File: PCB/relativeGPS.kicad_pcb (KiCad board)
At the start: 2 copper layers, 3 parts, among them CN1 PPPC051LGBN-RC, U1 TCA39306DCUR, U2 LSM303AH

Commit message: WIP
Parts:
- added ANT1: ANT2525B00DT1516S, 010-RF:ANT2525B00DT1516S, F.Cu at (139.9, 80.5)
- added C1: C_120pF_50V_5%_C0G_0402_H0.55, 002-Capacitors:C_0402_H0.55, F.Cu at (154.6, 68.3)
- added C10: C_1uF_50V_10%_X5R_0603_H0.9, 002-Capacitors:C_0603_H0.95, F.Cu at (173.0, 71.1)
- added C11: C_1uF_50V_10%_X5R_0603_H0.9, 002-Capacitors:C_0603_H0.95, F.Cu at (173.0, 73.6)
- added C12: C_100nF_50V_10%_X7R_0402_H0.55, 002-Capacitors:C_0402_H0.55, F.Cu at (163.7, 89.3)
- added C13: C_220nF_50V_10%_X7R_0603_H0.9, 002-Capacitors:C_0603_H0.95, F.Cu at (160.2, 87.5)
- added C14: C_10uF_10V_20%_X5R_0603H0.9, 002-Capacitors:C_0603_H0.95, F.Cu at (160.2, 90.0)
- added C2: C_4.7uF_10V_10%_X7S_0603_H0.95, 002-Capacitors:C_0603_H0.95, F.Cu at (148.5, 95.0)
- added C3: C_22uF_6.3V_20%_X5R_0805_H1.4, 002-Capacitors:C_0805_H1.4, F.Cu at (152.7, 95.2)
- added C4: C_120pF_50V_5%_C0G_0402_H0.55, 002-Capacitors:C_0402_H0.55, F.Cu at (154.6, 70.4)
- added C5: C_10nF_50V_10%_X7R_0402_H0.55, 002-Capacitors:C_0402_H0.55, F.Cu at (154.6, 72.5)
- added C6: C_56pF_50V_2%_C0G_0201_H0.33, 002-Capacitors:C_0402_H0.55, F.Cu at (154.6, 74.5)
- added C7: C_100nF_50V_10%_X7R_0402_H0.55, 002-Capacitors:C_0402_H0.55, F.Cu at (163.7, 87.3)
- added C8: C_100nF_50V_10%_X7R_0402_H0.55, 002-Capacitors:C_0402_H0.55, F.Cu at (159.7, 83.2)
- added C9: C_1uF_50V_10%_X5R_0603_H0.9, 002-Capacitors:C_0603_H0.95, F.Cu at (173.0, 68.6)
- added CN2: Solder_Jumper-2_Open, 009-Connectors:SolderJumper-2_Open, F.Cu at (148.7, 100.5)
- added IC1: MIC5330-SSYML-TR, 004-Power:MIC5330, F.Cu at (173.1, 81.8)
- added L1: L_5.6nH_2%_1.77A_40mOhm, 003-Inductors:LQW15AN5N6G80D, F.Cu at (152.3, 99.9)
- added L2: L_10uH_20%_1.51A_160mOhm, 003-Inductors:LTF5022T-100M1R3-D, F.Cu at (142.5, 97.1)
- added L3: L_27nH_5%_0.35A_460mOhm, 003-Inductors:LQG15HS27NJ02D, F.Cu at (152.2, 102.0)
- added R1: R_1M_5%_1/16W_0402, 001-Resistors:R_0402_H0.4, F.Cu at (154.6, 76.5)
- added R10: R_4k7_1%_1/10W_0603, 001-Resistors:R_0603_H0.55, F.Cu at (173.0, 78.6)
- added R2: R_0R_0603, 001-Resistors:R_0603_H0.55, F.Cu at (148.5, 97.5)
- added R3: R_68k_1%_1/16W_0402, 001-Resistors:R_0402_H0.4, F.Cu at (154.6, 78.6)
- added R4: R_15k_1%_1/16W_0402, 001-Resistors:R_0402_H0.4, F.Cu at (154.6, 80.7)
- added R5: R_4k7_1%_1/10W_0603, 001-Resistors:R_0603_H0.55, F.Cu at (160.2, 92.5)
- added R6: R_10k_5%_1/16W_0402, 001-Resistors:R_0402_H0.4, F.Cu at (154.6, 82.7)
- added R7: R_4k7_1%_1/10W_0603, 001-Resistors:R_0603_H0.55, F.Cu at (160.2, 95.1)
- added R8: R_200k_1%_1/16W_0402, 001-Resistors:R_0402_H0.4, F.Cu at (163.7, 91.4)
- added R9: R_4k7_1%_1/10W_0603, 001-Resistors:R_0603_H0.55, F.Cu at (173.0, 76.1)
- added U3: BGA725L6E6327FTSA1, 010-RF:BGA725L6E6327FTSA1, F.Cu at (152.2, 104.2)
- added U4: ST1S12GR, 004-Power:ST1S12GR, F.Cu at (140.7, 103.0)
- added U5: B39162B4327P810, 010-RF:B39162B4327P810, F.Cu at (148.0, 103.6)
- added U6: TESEO-LIV3R, 010-RF:TESEO-LIV3R, F.Cu at (132.5, 99.9)
- U1: value TCA39306DCUR -> LSM303AH; footprint 005-ICs:TCA39306DCUR -> 008-Sensors:LSM303AHTR
- U2: value LSM303AH -> TCA39306DCUR; footprint 008-Sensors:LSM303AHTR -> 005-ICs:TCA39306DCUR
- moved U1 30.4 mm to (167.1, 88.2)
- moved U2 28.1 mm to (164.9, 94.2)
- moved CN1 22.0 mm to (160.0, 74.8)
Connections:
- net /SDA_1V8 renamed /MAG_ACC/LSM_SDA
- CN1 pad 1: +3.3V -> +3.3V_RYLR
- U1 pad 1: GND -> /MAG_ACC/LSM_SCL
- U1 pad 3: /SCL_1V8 -> unconnected-(U1-NC-Pad3)
- U1 pad 5: unconnected-(U1-SDA2-Pad5) -> Net-(U1-C1)
- U1 pad 6: unconnected-(U1-SCL2-Pad6) -> GND
- U1 pad 7: unconnected-(U1-VREF2-Pad7) -> /MAG_ACC_DRDY
- U1 pad 8: unconnected-(U1-EN-Pad8) -> GND
- U2 pad 1: /SCL_1V8 -> GND
- U2 pad 3: unconnected-(U2-NC-Pad3) -> /MAG_ACC/LSM_SCL
- U2 pad 5: unconnected-(U2-C1-Pad5) -> /SDA
- U2 pad 6: GND -> /SCL
- U2 pad 7: unconnected-(U2-DRDY/MAG_INT-Pad7) -> Net-(U2-EN)
- U2 pad 8: GND -> Net-(U2-EN)

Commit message: WIP
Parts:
- added U7: AAA_2X_Holder, 004-Power:AAA_2X_Holder, B.Cu at (147.8, 100.0)
- C6, U6: moved to B.Cu
- C8: value C_100nF_50V_10%_X7R_0402_H0.55 -> C_1uF_50V_10%_X5R_0603_H0.9; footprint 002-Capacitors:C_0402_H0.55 -> 002-Capacitors:C_0603_H0.95
- C9: value C_1uF_50V_10%_X5R_0603_H0.9 -> C_100nF_50V_10%_X7R_0402_H0.55; footprint 002-Capacitors:C_0603_H0.95 -> 002-Capacitors:C_0402_H0.55
- CN1: value PPPC051LGBN-RC -> 5PTH_connector; footprint 009-Connectors:PPPC051LGBN-RC -> 009-Connectors:5-PTH_connector
- moved C1 85.1 mm to (239.1, 78.6)
- moved C10 85.1 mm to (257.5, 81.3)
- moved C11 85.1 mm to (257.5, 83.8)
- moved C12 85.1 mm to (248.2, 99.6)
- moved C13 85.1 mm to (244.6, 97.8)
- moved C14 85.1 mm to (244.6, 100.3)
- moved C3 85.1 mm to (237.2, 105.5)
- moved C4 85.1 mm to (239.1, 80.6)
- moved C5 85.1 mm to (239.1, 82.7)
- moved C7 85.1 mm to (248.2, 97.5)
- moved C8 85.1 mm to (244.1, 93.5)
- moved C9 85.1 mm to (257.5, 78.8)
- moved CN2 85.1 mm to (233.1, 110.8)
- moved IC1 85.1 mm to (257.5, 92.0)
- moved L1 85.1 mm to (236.8, 110.1)
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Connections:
- C8 pad 1: Net-(IC1-BYP) -> +5V
- C9 pad 1: +5V -> Net-(IC1-BYP)
- IC1 pad 9: (no net) -> GND
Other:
- board outline added: 60 x 60 mm

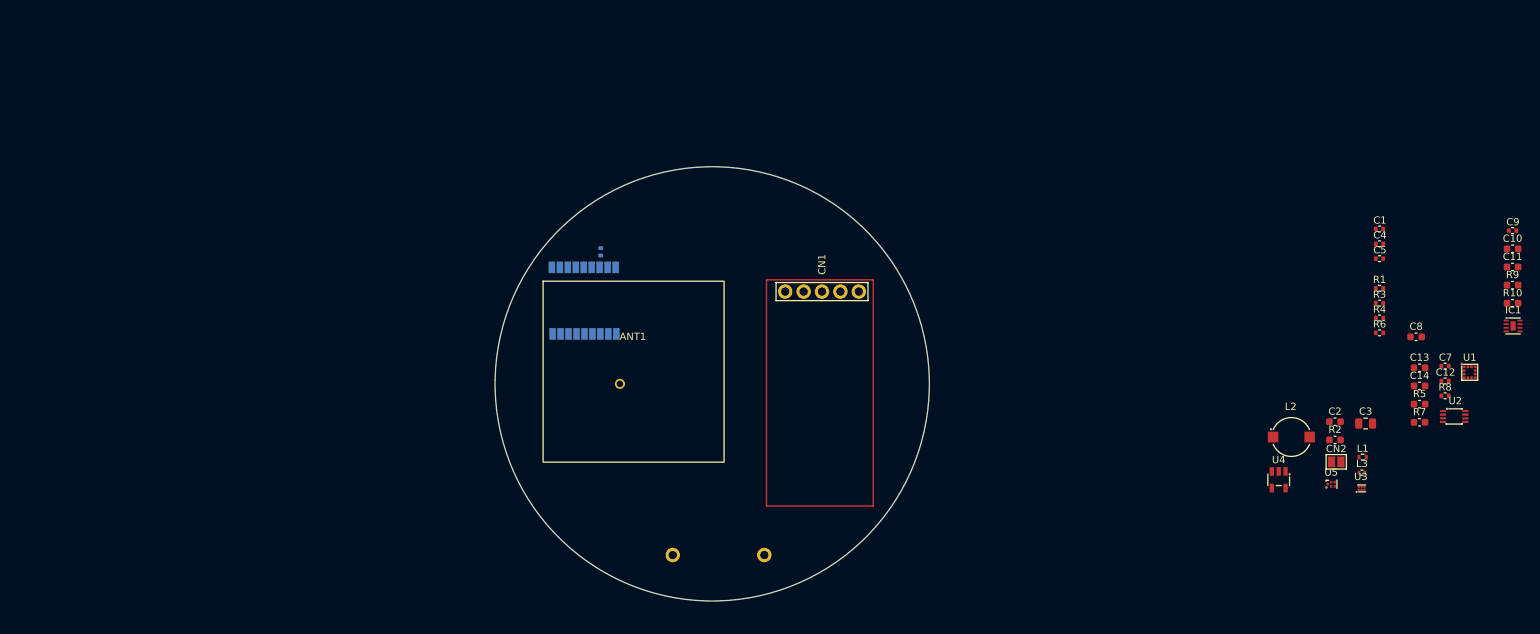
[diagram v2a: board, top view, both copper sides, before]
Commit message: Add LEDs
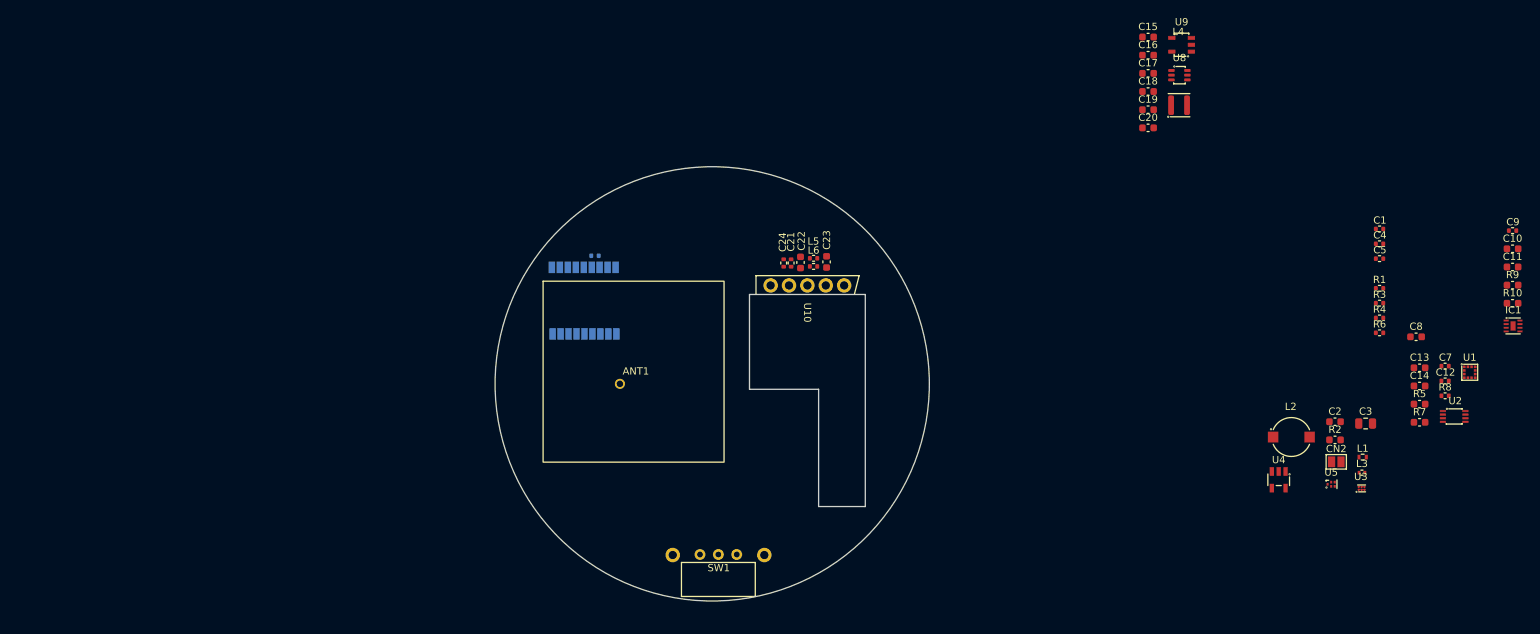
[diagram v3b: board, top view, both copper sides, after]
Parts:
- removed CN1: 5PTH_connector, 009-Connectors:5-PTH_connector
- added C15: C_4.7uF_10V_10%_X7S_0603_H0.95, 002-Capacitors:C_0603_H0.95, F.Cu at (207.1, 52.1)
- added C16: C_1uF_50V_10%_X5R_0603_H0.9, 002-Capacitors:C_0603_H0.95, F.Cu at (207.1, 54.6)
- added C17: C_10uF_10V_20%_X5R_0603H0.9, 002-Capacitors:C_0603_H0.95, F.Cu at (207.1, 57.1)
- added C18: C_100pF_50V_5%_C0G_0603_H0.9, 002-Capacitors:C_0603_H0.95, F.Cu at (207.1, 59.6)
- added C19: C_22uF_25V_20%_X5S_0603_H1, 002-Capacitors:C_0603_H0.95, F.Cu at (207.1, 62.1)
- added C20: C_22uF_25V_20%_X5S_0603_H1, 002-Capacitors:C_0603_H0.95, F.Cu at (207.1, 64.6)
- added C21: C_100nF_50V_10%_X7R_0402_H0.55, 002-Capacitors:C_0402_H0.55, F.Cu at (157.8, 83.3)
- added C22: C_10uF_10V_20%_X5R_0603H0.9, 002-Capacitors:C_0603_H0.95, F.Cu at (159.1, 83.2)
- added C23: C_10uF_10V_20%_X5R_0603H0.9, 002-Capacitors:C_0603_H0.95, F.Cu at (162.7, 83.2)
- added C24: C_47pF_50V_5%_C0G_0402, 002-Capacitors:C_0402_H0.55, F.Cu at (156.8, 83.3)
- added L4: L_4.7uH_20%_850mA_168mOhm, 003-Inductors:LQH3NPZ4R7MGRL, F.Cu at (211.4, 61.5)
- added L5: FERR_120R@100MHz_5%_1.5A_95mOhm, 003-Inductors:FERR_0402_H0.55, F.Cu at (160.9, 82.7)
- added L6: FERR_120R@100MHz_5%_1.5A_95mOhm, 003-Inductors:FERR_0402_H0.55, F.Cu at (160.9, 83.8)
- added SW1: switch_slide_2pos, 009-Connectors:09.10290.01, F.Cu at (147.8, 123.6)
- added U10: RYLR998, 010-RF:RYLR998_flat, F.Cu at (160.1, 86.4)
- added U8: TPS61222DCKR, 004-Power:TPS61222DCKR, F.Cu at (211.4, 57.4)
- added U9: TPS79318DBVR, 004-Power:TPS79318DBVR, F.Cu at (211.8, 53.1)
- moved C6 0.97 mm to (130.7, 82.3), turned to 180 degrees
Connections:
- net /GPS/3V3_TESEO renamed +3.3V_TESEO
- net /RYLR_3V3_EN renamed /3V3_RYLR_EN

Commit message: WIP
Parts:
- added C25: C_22uF_25V_20%_X5S_0603_H1, 002-Capacitors:C_0603_H0.95, F.Cu at (106.0, 69.2)
- added C26: C_2.2uF_25V_25%_X5R_0402_H0.55, 002-Capacitors:C_0402_H0.55, F.Cu at (88.1, 97.1)
- added C27: C_100nF_50V_10%_X7R_0402_H0.55, 002-Capacitors:C_0402_H0.55, F.Cu at (88.1, 99.2)
- added CN1: FTSH-107-01-L-DV-K-P-TR, 009-Connectors:FTSH-107-01-L-DV-K-P-TR, F.Cu at (103.2, 100.3)
- added CN3: TC2030-IDC, 009-Connectors:Debug_pads_6pin, F.Cu at (104.4, 107.3)
- added CN4: 5033981892, 009-Connectors:Micro_SD_5033981892, F.Cu at (79.0, 104.0)
- added D1: COM-16347, 006-Diodes:COM-16347, F.Cu at (75.5, 71.2)
- added D10: COM-16347, 006-Diodes:COM-16347, F.Cu at (91.4, 77.7)
- added D11: COM-16347, 006-Diodes:COM-16347, F.Cu at (91.4, 84.3)
- added D2: COM-16347, 006-Diodes:COM-16347, F.Cu at (75.5, 77.7)
- added D3: COM-16347, 006-Diodes:COM-16347, F.Cu at (75.5, 84.3)
- added D4: COM-16347, 006-Diodes:COM-16347, F.Cu at (75.5, 90.8)
- added D5: COM-16347, 006-Diodes:COM-16347, F.Cu at (83.4, 71.2)
- added D6: COM-16347, 006-Diodes:COM-16347, F.Cu at (83.4, 77.7)
- added D7: COM-16347, 006-Diodes:COM-16347, F.Cu at (83.4, 84.3)
- added D8: COM-16347, 006-Diodes:COM-16347, F.Cu at (83.4, 90.8)
- added D9: COM-16347, 006-Diodes:COM-16347, F.Cu at (91.4, 71.2)
- added R11: R_100k_1%_1/16W_0402, 001-Resistors:R_0402_H0.4, F.Cu at (88.1, 101.2)
- added R12: R_100k_1%_1/16W_0402, 001-Resistors:R_0402_H0.4, F.Cu at (88.1, 103.3)
- added R13: R_100k_1%_1/16W_0402, 001-Resistors:R_0402_H0.4, F.Cu at (88.1, 105.3)
- added R14: R_100k_1%_1/16W_0402, 001-Resistors:R_0402_H0.4, F.Cu at (88.1, 107.4)
- added SW2: EVQ-P7A01P, 009-Connectors:EVQ-P7A01P, F.Cu at (94.7, 98.5)
- added SW3: EVQ-P7A01P, 009-Connectors:EVQ-P7A01P, F.Cu at (94.7, 103.6)
- added TP1: TP_square_1mm, 011-Misc:Testpoint_square_1mm, F.Cu at (98.9, 105.5)
- added TP10: TP_square_1mm, 011-Misc:Testpoint_square_1mm, F.Cu at (103.0, 70.9)
- added TP11: TP_square_1mm, 011-Misc:Testpoint_square_1mm, F.Cu at (98.9, 107.5)
- added TP12: TP_square_1mm, 011-Misc:Testpoint_square_1mm, F.Cu at (98.9, 109.5)
- added TP2: TP_square_1mm, 011-Misc:Testpoint_square_1mm, F.Cu at (96.4, 72.4)
- added TP3: TP_square_1mm, 011-Misc:Testpoint_square_1mm, F.Cu at (87.6, 109.4)
- added TP4: TP_square_1mm, 011-Misc:Testpoint_square_1mm, F.Cu at (107.0, 74.9)
- added TP5: TP_square_1mm, 011-Misc:Testpoint_square_1mm, F.Cu at (107.0, 76.9)
- added TP6: TP_square_1mm, 011-Misc:Testpoint_square_1mm, F.Cu at (103.0, 74.9)
- added TP7: TP_square_1mm, 011-Misc:Testpoint_square_1mm, F.Cu at (103.0, 76.9)
- added TP8: TP_square_1mm, 011-Misc:Testpoint_square_1mm, F.Cu at (103.0, 78.9)
- added TP9: TP_square_1mm, 011-Misc:Testpoint_square_1mm, F.Cu at (103.0, 68.9)
- added U11: 74LVC1T45GW,125, 005-ICs:TSSOP6_SOT363-2.step, F.Cu at (97.7, 69.7)
- R10, R9: value R_4k7_1%_1/10W_0603 -> R_DNP_0402; footprint 001-Resistors:R_0603_H0.55 -> 001-Resistors:R_0402_H0.4
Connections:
- C11 pad 1: +3.3V_RYLR -> +3.3V
- C15 pad 1: +VBAT -> +3V8
- C16 pad 1: +VBAT_ON -> +3V8
- C20 pad 1: +VBAT_ON -> +3V8
- C23 pad 1: +3.3V_RYLR -> +3.3V
- C3 pad 1: +3.3V_TESEO -> +3.3V
- C5 pad 1: +3.3V_TESEO -> +3.3V
- IC1 pad 7: +3.3V_RYLR -> +3.3V
- L2 pad 2: +3.3V_TESEO -> +3.3V
- L3 pad 1: +3.3V_TESEO -> +3.3V
- L4 pad 1: +VBAT_ON -> +3V8
- L5 pad 1: +3.3V_RYLR -> +3.3V
- R10 pad 2: /SDA -> /SCL
- R9 pad 2: /SCL -> /SDA
- SW1 pad 1: +VBAT_ON -> +3V8
- SW1 pad 2: +VBAT -> +3V8
- U7 pad 1: +VBAT -> +3V8
- U8 pad 1: +VBAT_ON -> +3V8
- U8 pad 6: +VBAT_ON -> +3V8
- U9 pad 1: +VBAT_ON -> +3V8

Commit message: Layout start
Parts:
- removed IC1: MIC5330-SSYML-TR, 004-Power:MIC5330
- removed TP1, TP10, TP11, TP12, TP2, TP3, TP4, TP5, TP6, TP7, TP8, TP9: TP_square_1mm, 011-Misc:Testpoint_square_1mm
- added B7: AAA_2X_Holder, 004-Power:AAA_2X_Holder, B.Cu at (100.0, 99.2)
- added C28: C_10nF_50V_10%_X7R_0402_H0.55, 002-Capacitors:C_0402_H0.55, B.Cu at (70.5, 103.7)
- added C29: C_100nF_50V_10%_X7R_0402_H0.55, 002-Capacitors:C_0402_H0.55, B.Cu at (72.8, 111.4)
- added C30: C_2.2uF_25V_25%_X5R_0402_H0.55, 002-Capacitors:C_0402_H0.55, F.Cu at (109.7, 73.7)
- added C31: C_100nF_50V_10%_X7R_0402_H0.55, 002-Capacitors:C_0402_H0.55, B.Cu at (74.8, 116.2)
- added C32: C_100nF_50V_10%_X7R_0402_H0.55, 002-Capacitors:C_0402_H0.55, B.Cu at (73.4, 109.0)
- added C33: C_100nF_50V_10%_X7R_0402_H0.55, 002-Capacitors:C_0402_H0.55, B.Cu at (77.6, 103.7)
- added C34: C_100nF_50V_10%_X7R_0402_H0.55, 002-Capacitors:C_0402_H0.55, B.Cu at (84.1, 103.7)
- added C35: C_100nF_50V_10%_X7R_0402_H0.55, 002-Capacitors:C_0402_H0.55, B.Cu at (87.9, 114.5)
- added C36: C_10uF_10V_20%_X5R_0402_H0.55, 002-Capacitors:C_0402_H0.55, B.Cu at (88.9, 114.5)
- added R15: R_0R_1%_1/16W_0402, 001-Resistors:R_0402_H0.4, B.Cu at (85.7, 74.0)
- added SW4: TL3315NF160Q, 009-Connectors:TL3315NF160Q, B.Cu at (70.5, 100.0)
- added U12: ASE-8.000MHZ-L-C-T, 005-ICs:ASE-8.000MHZ-L-C-T, B.Cu at (70.6, 106.2)
- added U13: MIC5330-SSYML-TR, 004-Power:MIC5330, F.Cu at (103.9, 112.3)
- C1, C26, C27, C4, C5, CN1, CN2, CN3, L1, L3, R11, R12, R13, R14, R2, R6, U3, U5: moved to B.Cu
- C10, C11, C8: value C_1uF_50V_10%_X5R_0603_H0.9 -> C_1uF_50V_10%_X5R_0402_H0.55; footprint 002-Capacitors:C_0603_H0.95 -> 002-Capacitors:C_0402_H0.55
- C13: value C_220nF_50V_10%_X7R_0603_H0.9 -> C_2.2uF_25V_25%_X5R_0402_H0.55; footprint 002-Capacitors:C_0603_H0.95 -> 002-Capacitors:C_0402_H0.55
- C14: value C_10uF_10V_20%_X5R_0603H0.9 -> C_220nF_16V_10%_X7R_0402_H0.55; footprint 002-Capacitors:C_0603_H0.95 -> 002-Capacitors:C_0402_H0.55
- C17: value C_10uF_10V_20%_X5R_0603H0.9 -> C_100nF_50V_10%_X7R_0402_H0.55; footprint 002-Capacitors:C_0603_H0.95 -> 002-Capacitors:C_0402_H0.55; moved to B.Cu
- R5, R7: value R_4k7_1%_1/10W_0603 -> R_4k7_5%_1/16W_0402; footprint 001-Resistors:R_0603_H0.55 -> 001-Resistors:R_0402_H0.4
- U11: value 74LVC1T45GW,125 -> STM32L431RCT6TR; footprint 005-ICs:TSSOP6_SOT363-2.step -> 007-MCUs:LQFP-64_10x10mm_P0.5mm; moved to B.Cu
- U7: value AAA_2X_Holder -> 74LVC1T45GW.125; footprint 004-Power:AAA_2X_Holder -> 005-ICs:TSSOP6_SOT363-2.step; moved to F.Cu
- moved R9 159.4 mm to (98.5, 74.3), turned to -90 degrees
- moved C10 158.4 mm to (102.0, 111.6), turned to -90 degrees
- moved R10 158.3 mm to (99.7, 76.1), turned to 90 degrees
- moved C9 157.4 mm to (104.1, 114.3), turned to 180 degrees
- moved L3 155.7 mm to (84.8, 77.9), turned to 180 degrees
- moved C1 155.7 mm to (84.8, 99.2), turned to 90 degrees
- moved C11 155.5 mm to (104.2, 110.1)
- moved R6 154.8 mm to (84.3, 91.9), turned to 90 degrees
- moved C4 154.2 mm to (85.3, 91.9), turned to 90 degrees
- moved CN2 153.2 mm to (80.9, 93.5), turned to -90 degrees
- moved U3 152.8 mm to (85.0, 95.6)
- moved C5 152.8 mm to (86.4, 78.4), turned to -90 degrees
- moved L1 152.3 mm to (85.0, 97.2), turned to 90 degrees
- moved R2 150.6 mm to (83.0, 93.5), turned to 90 degrees
- moved U2 149.6 mm to (102.7, 74.9), turned to 180 degrees
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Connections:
- C11 pad 1: +3.3V -> +3.3V_LORA
- C13 pad 1: Net-(U1-C1) -> +1V8
- C14 pad 1: +1V8 -> Net-(U1-C1)
- C15 pad 1: +3V8 -> +BATT
- C16 pad 1: +3V8 -> +3V0
- C17 pad 1: +1V8 -> +3.3V
- C20 pad 1: +3V8 -> +3V0
- C23 pad 1: +3.3V -> +3.3V_LORA
- C3 pad 1: +3.3V -> +3.3V_GPS
- C5 pad 1: +3.3V -> +3.3V_GPS
- CN3 pad 6: /SWO -> unconnected-(CN3-SWO-Pad6)
- CN4 pad 5: /SD_CLK -> Net-(CN4-CLK)
- L2 pad 2: +3.3V -> +3.3V_GPS
- L3 pad 1: +3.3V -> +3.3V_GPS
- L4 pad 1: +3V8 -> +3V0
- L5 pad 1: +3.3V -> +3.3V_LORA
- SW1 pad 1: +3V8 -> unconnected-(SW1-Pad1)
- SW1 pad 2: +3V8 -> +BATT
- SW1 pad 3: unconnected-(SW1-Pad3) -> +3V0
- U11 pad 1: +3V3 -> +3.3V
- U11 pad 2: GND -> unconnected-(U11-PC13-Pad2)
- U11 pad 3: /LED_DATA -> unconnected-(U11-PC14-OSC32_IN-Pad3)
- U11 pad 4: Net-(D1-DIN) -> unconnected-(U11-PC15-OSC32_OUT-Pad4)
- U11 pad 5: +3V3 -> Net-(U11-PH0-OSC_IN)
- U11 pad 6: +5V -> unconnected-(U11-PH1-OSC_OUT-Pad6)
- U7 pad 1: +3V8 -> +3V3
- U8 pad 1: +3V8 -> +3V0
- U8 pad 6: +3V8 -> +3V0
- U9 pad 1: +3V8 -> +3V0
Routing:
- net +5V: track 0.00 -> 227.8 mm, vias 0 -> 4
- net GND: track 0.00 -> 129.8 mm, vias 0 -> 67
- net /NRST: track 0.00 -> 100.7 mm, vias 0 -> 2
- net /UART_TX: track 0.00 -> 87.9 mm, vias 0 -> 4
- net /UART_RX: track 0.00 -> 87.3 mm, vias 0 -> 4
- net /BUTTON_2: track 0.00 -> 84.1 mm, vias 0 -> 1
- net /SWDIO: track 0.00 -> 72.5 mm, vias 0 -> 2
- net /SWCLK: track 0.00 -> 67.4 mm, vias 0 -> 6
- net /SD_DAT3: track 0.00 -> 66.3 mm, vias 0 -> 3
- net /SD_DAT2: track 0.00 -> 63.0 mm, vias 0 -> 3
- net /RYLR998_TX: track 0.00 -> 55.2 mm, vias 0 -> 1
- net /RYLR998_RX: track 0.00 -> 52.7 mm
- net /RYLR998_NRST: track 0.00 -> 50.1 mm
- net /SD_DAT1: track 0.00 -> 45.8 mm, vias 0 -> 1
- net /SD_DAT0: track 0.00 -> 44.6 mm, vias 0 -> 1
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- added copper zone on F.Cu, net +5V
- added copper zone on F.Cu, net GND
- added copper zone on In1.Cu, net GND
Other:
- board size 60 x 60 mm -> 65 x 65 mm
- copper layers 2 -> 4

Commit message: First layout draft
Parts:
- moved C36 15.3 mm to (73.7, 116.2), turned to -90 degrees
- moved C35 2.05 mm to (86.9, 116.3), turned to -90 degrees
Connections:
- C26 pad 1: +3V3 -> +3.3V
- C27 pad 1: +3V3 -> +3.3V
- CN4 pad 4: +3V3 -> +3.3V
- R11 pad 1: +3V3 -> +3.3V
- R12 pad 1: +3V3 -> +3.3V
- R13 pad 1: +3V3 -> +3.3V
- R14 pad 1: +3V3 -> +3.3V
- U11 pad 21: unconnected-(U11-PA5-Pad21) -> /BUTTON_1
- U11 pad 33: unconnected-(U11-PB12-Pad33) -> /3V3_RYLR_EN
- U11 pad 34: unconnected-(U11-PB13-Pad34) -> /MAG_ACC_DRDY
- U11 pad 35: unconnected-(U11-PB14-Pad35) -> /MAG_ACC_INT1
- U11 pad 37: unconnected-(U11-PC6-Pad37) -> /MAG_ACC_INT2
- U11 pad 38: unconnected-(U11-PC7-Pad38) -> /3V3_TESEO_EN
- U11 pad 41: unconnected-(U11-PA8-Pad41) -> /SD_DETECT
- U11 pad 45: unconnected-(U11-PA12-Pad45) -> /1V8_ACC_MAG_EN
- U11 pad 56: /SD_DETECT -> unconnected-(U11-PB4-Pad56)
- U7 pad 1: +3V3 -> +3.3V
- U7 pad 5: +3V3 -> +3.3V
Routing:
- net +3.3V: track 32.3 -> 220.0 mm, vias 6 -> 13
- net /MAG_ACC_INT2: track 0.00 -> 52.5 mm, vias 0 -> 3
- net /MAG_ACC_DRDY: track 0.00 -> 52.5 mm, vias 0 -> 1
- net /MAG_ACC_INT1: track 0.00 -> 50.5 mm, vias 0 -> 3
- net /1V8_ACC_MAG_EN: track 0.00 -> 49.3 mm, vias 0 -> 3
- net /SD_CMD: track 0.00 -> 49.1 mm, vias 0 -> 1
- net /SD_CLK: track 0.00 -> 47.2 mm
- net /3V3_TESEO_EN: track 0.00 -> 45.4 mm, vias 0 -> 3
- net +3V0: track 18.5 -> 61.9 mm, vias 0 -> 2
- net +3.3V_LORA: track 1.19 -> 43.4 mm, vias 0 -> 2
- net +3.3V_GPS: track 1.20 -> 40.2 mm, vias 0 -> 2
- net /3V3_RYLR_EN: track 0.00 -> 34.9 mm, vias 0 -> 3
- net /SD_DETECT: track 0.00 -> 31.7 mm, vias 0 -> 1
- net /SCL: track 38.7 -> 68.3 mm, vias 2 -> 4
- net /SDA: track 40.9 -> 70.0 mm, vias 2 -> 4
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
